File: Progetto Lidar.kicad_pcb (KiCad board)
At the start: 2 copper layers, 2 parts

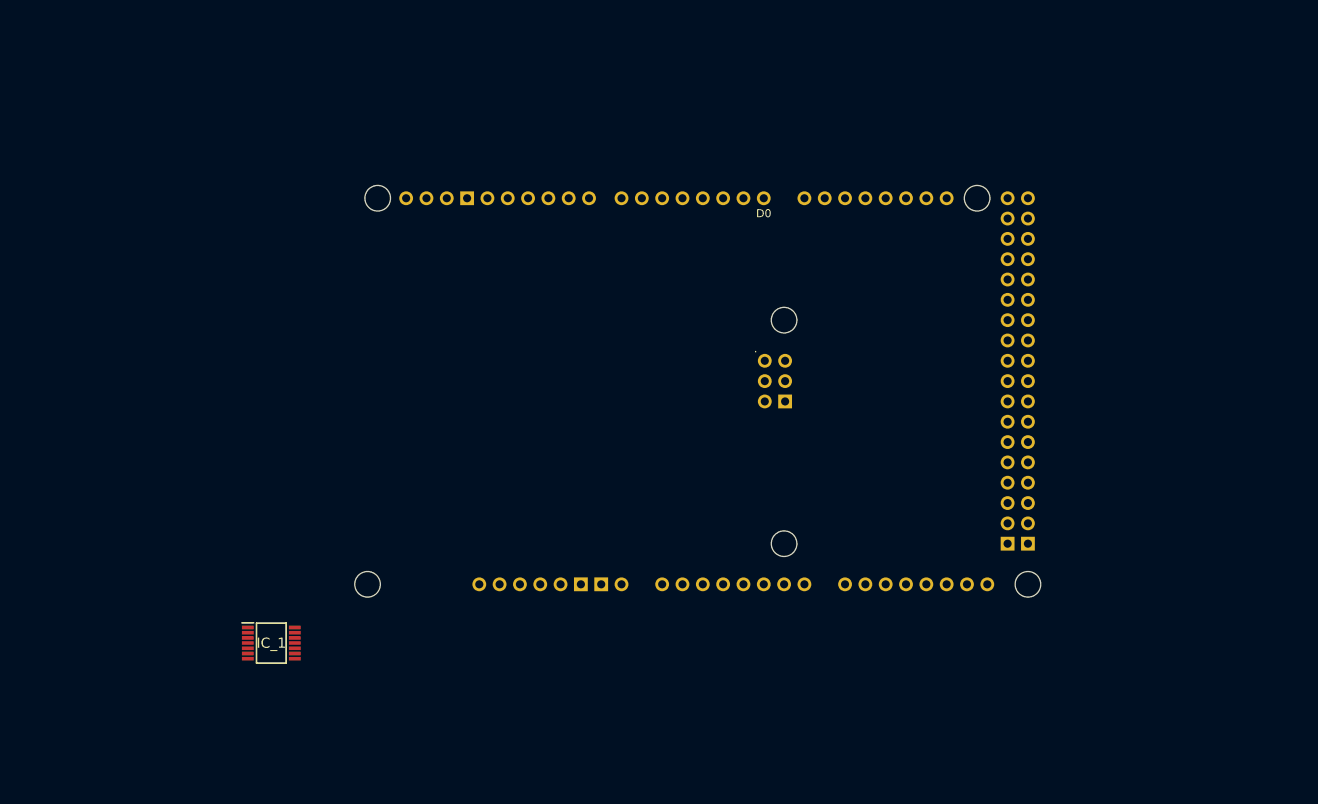
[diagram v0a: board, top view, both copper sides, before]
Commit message: Finito lo schematico e aggiunto modelli 3D
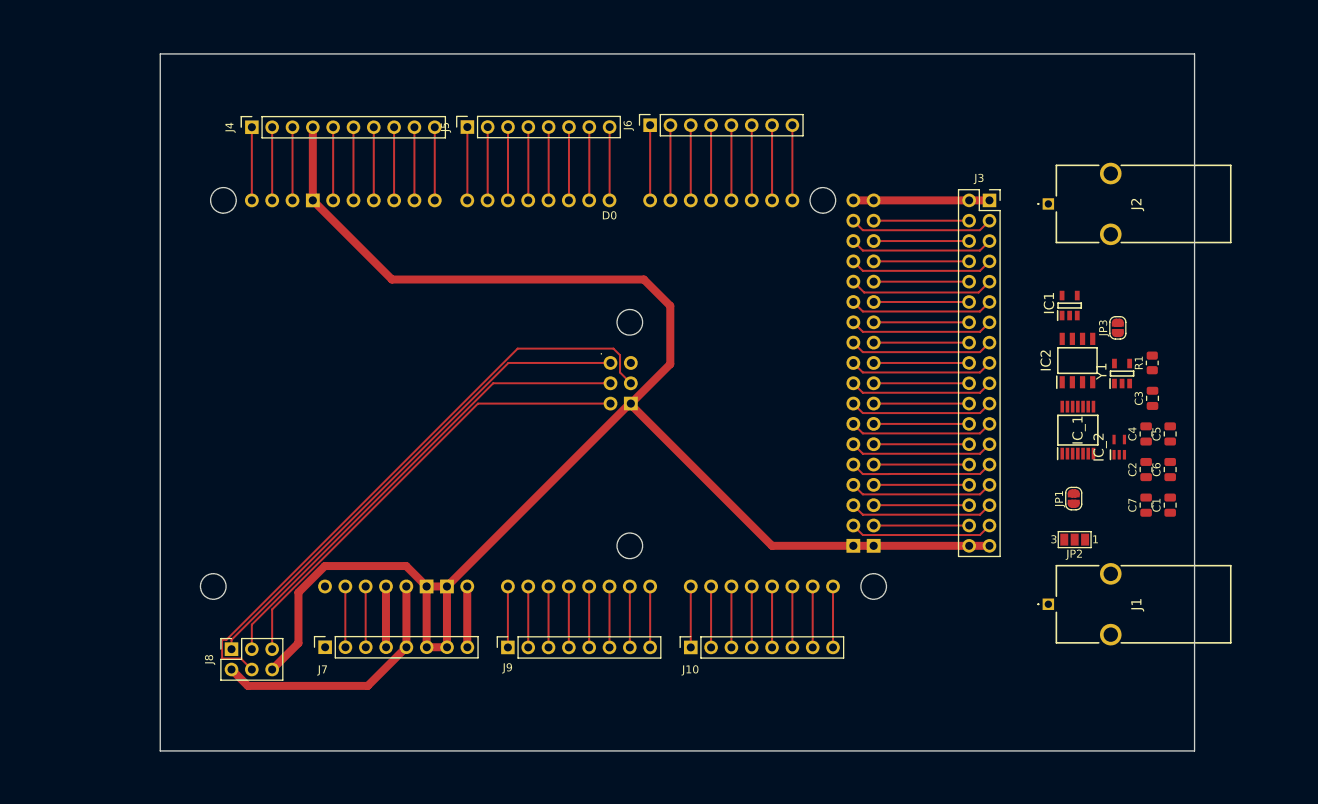
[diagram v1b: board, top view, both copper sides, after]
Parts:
- added C1: 0.1uF, Capacitor_SMD:C_0805_2012Metric, F.Cu at (207.8, 101.9)
- added C2: 1uF, Capacitor_SMD:C_0805_2012Metric, F.Cu at (204.8, 97.4)
- added C3: 100nF, Capacitor_SMD:C_0805_2012Metric, F.Cu at (205.6, 88.5)
- added C4: 1uF, Capacitor_SMD:C_0805_2012Metric, F.Cu at (204.8, 93.0)
- added C5: 100nF, Capacitor_SMD:C_0805_2012Metric, F.Cu at (207.8, 93.0)
- added C6: 100nF, Capacitor_SMD:C_0805_2012Metric, F.Cu at (207.8, 97.4)
- added C7: 100nF, Capacitor_SMD:C_0805_2012Metric, F.Cu at (204.8, 101.9)
- added IC1: TLV74133PDBVR, Libreria_componenti_footprint:SOT95P280X145-5N, F.Cu at (195.2, 76.9)
- added IC2: LM393BIDR, Libreria_componenti_footprint:SOIC127P600X175-8N, F.Cu at (196.2, 83.8)
- added IC_2: SN74LVC1G125DCKR, Libreria_componenti_footprint:SOT65P210X110-5N, F.Cu at (201.4, 94.6)
- added J1: CONN_LASER, Libreria_componenti_footprint:731713150, F.Cu at (192.5, 114.3)
- added J10: Conn_01x08, Connector_PinSocket_2.54mm:PinSocket_1x08_P2.54mm_Vertical, F.Cu at (147.8, 119.6)
- added J2: Conn_Coaxial, Libreria_componenti_footprint:731713150, F.Cu at (192.5, 64.2)
- added J3: Conn_02x18_Odd_Even, Connector_PinSocket_2.54mm:PinSocket_2x18_P2.54mm_Vertical, F.Cu at (185.2, 63.8)
- added J4: Conn_01x10, Connector_PinSocket_2.54mm:PinSocket_1x10_P2.54mm_Vertical, F.Cu at (93.0, 54.6)
- added J5: Conn_01x08, Connector_PinSocket_2.54mm:PinSocket_1x08_P2.54mm_Vertical, F.Cu at (119.9, 54.6)
- added J6: Conn_01x08, Connector_PinSocket_2.54mm:PinSocket_1x08_P2.54mm_Vertical, F.Cu at (142.8, 54.4)
- added J7: Conn_01x08, Connector_PinSocket_2.54mm:PinSocket_1x08_P2.54mm_Vertical, F.Cu at (102.1, 119.6)
- added J8: Conn_SPI, Connector_PinSocket_2.54mm:PinSocket_2x03_P2.54mm_Vertical, F.Cu at (90.4, 119.9)
- added J9: Conn_01x08, Connector_PinSocket_2.54mm:PinSocket_1x08_P2.54mm_Vertical, F.Cu at (125.0, 119.6)
- added JP1: REG_EN, Jumper:SolderJumper-2_P1.3mm_Open_RoundedPad1.0x1.5mm, F.Cu at (195.7, 101.0)
- added JP2: SolderJumper_3_Open, Jumper:SolderJumper-3_P1.3mm_Open_Pad1.0x1.5mm_NumberLabels, F.Cu at (195.8, 106.2)
- added JP3: OSC_EN, Jumper:SolderJumper-2_P1.3mm_Open_RoundedPad1.0x1.5mm, F.Cu at (201.2, 79.7)
- added R1: 10k, Resistor_SMD:R_0805_2012Metric, F.Cu at (205.5, 84.1)
- added Y1: SiT2024BA-S2-33E-8.000000G, Libreria_componenti_footprint:SOT95P280X145-5N, F.Cu at (201.8, 85.4)
- moved IC_1 104.3 mm to (196.2, 92.5), turned to 90 degrees
- moved A1 19.3 mm to (74.2, 114.6)
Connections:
- A1 pad 3V3: unconnected-(A1-Pad3V3) -> /3V3_ARDUINO
- A1 pad 5V1: unconnected-(A1-Pad5V1) -> +5V
- A1 pad 5V2: unconnected-(A1-Pad5V2) -> +5V
- A1 pad 5V3: unconnected-(A1-Pad5V3) -> +5V
- A1 pad 5V4: unconnected-(A1-Pad5V4) -> +5V
- A1 pad A0: unconnected-(A1-PadA0) -> /ARD_AN_A0
- A1 pad A1: unconnected-(A1-PadA1) -> /ARD_AN_A1
- A1 pad A10: unconnected-(A1-PadA10) -> /ARD_AN_A10
- A1 pad A11: unconnected-(A1-PadA11) -> /ARD_AN_A11
- A1 pad A2: unconnected-(A1-PadA2) -> /ARD_AN_A2
- A1 pad A3: unconnected-(A1-PadA3) -> /ARD_AN_A3
- A1 pad A4: unconnected-(A1-PadA4) -> /ARD_AN_A4
- A1 pad A5: unconnected-(A1-PadA5) -> /ARD_AN_A5
- A1 pad A6: unconnected-(A1-PadA6) -> /ARD_AN_A6
- A1 pad A7: unconnected-(A1-PadA7) -> /ARD_AN_A7
- A1 pad A8: unconnected-(A1-PadA8) -> /ARD_AN_A8
- A1 pad A9: unconnected-(A1-PadA9) -> /ARD_AN_A9
- A1 pad AREF: unconnected-(A1-PadAREF) -> /ARD_AN_AREF
- A1 pad CANR: unconnected-(A1-PadCANR) -> /ARD_CAN_RX
- A1 pad CANT: unconnected-(A1-PadCANT) -> /ARD_CAN_TX
- A1 pad D0: unconnected-(A1-PadD0) -> /ARD_SR_RX0
- A1 pad D1: unconnected-(A1-PadD1) -> /ARD_SR_TX0
- A1 pad D10: unconnected-(A1-PadD10) -> /ARD_GPIO_D10
- A1 pad D11: unconnected-(A1-PadD11) -> /ARD_GPIO_D11
- A1 pad D12: unconnected-(A1-PadD12) -> /ARD_GPIO_D12
- A1 pad D13: unconnected-(A1-PadD13) -> /ARD_GPIO_D13
- A1 pad D14: unconnected-(A1-PadD14) -> /ARD_SR_TX3
- A1 pad D15: unconnected-(A1-PadD15) -> /ARD_SR_RX3
- A1 pad D16: unconnected-(A1-PadD16) -> /ARD_SR_TX2
- A1 pad D17: unconnected-(A1-PadD17) -> /ARD_SR_RX2
- A1 pad D18: unconnected-(A1-PadD18) -> /ARD_SR_TX1
- A1 pad D19: unconnected-(A1-PadD19) -> /ARD_SR_RX1
- A1 pad D2: unconnected-(A1-PadD2) -> /SPI_CS
- A1 pad D20: unconnected-(A1-PadD20) -> /ARD_I2C_SDA
- A1 pad D21: unconnected-(A1-PadD21) -> /ARD_I2C_SCL
- A1 pad D22: unconnected-(A1-PadD22) -> /ARD_GPIO_D22
- A1 pad D23: unconnected-(A1-PadD23) -> /ARD_GPIO_D23
- A1 pad D24: unconnected-(A1-PadD24) -> /ARD_GPIO_D24
- A1 pad D25: unconnected-(A1-PadD25) -> /ARD_GPIO_D25
- A1 pad D26: unconnected-(A1-PadD26) -> /ARD_GPIO_D26
- A1 pad D27: unconnected-(A1-PadD27) -> /ARD_GPIO_D27
- A1 pad D28: unconnected-(A1-PadD28) -> /ARD_GPIO_D28
- A1 pad D29: unconnected-(A1-PadD29) -> /ARD_GPIO_D29
- A1 pad D3: unconnected-(A1-PadD3) -> /ARD_V_REF
- A1 pad D30: unconnected-(A1-PadD30) -> /ARD_GPIO_D30
- A1 pad D31: unconnected-(A1-PadD31) -> /ARD_GPIO_D31
- A1 pad D32: unconnected-(A1-PadD32) -> /ARD_GPIO_D32
- A1 pad D33: unconnected-(A1-PadD33) -> /ARD_GPIO_D33
- A1 pad D34: unconnected-(A1-PadD34) -> /ARD_GPIO_D34
- A1 pad D35: unconnected-(A1-PadD35) -> /ARD_GPIO_D35
- A1 pad D36: unconnected-(A1-PadD36) -> /ARD_GPIO_D36
- A1 pad D37: unconnected-(A1-PadD37) -> /ARD_GPIO_D37
- A1 pad D38: unconnected-(A1-PadD38) -> /ARD_GPIO_D38
- A1 pad D39: unconnected-(A1-PadD39) -> /ARD_GPIO_D39
- A1 pad D4: unconnected-(A1-PadD4) -> /ARD_TRIG
- A1 pad D40: unconnected-(A1-PadD40) -> /ARD_GPIO_D40
- A1 pad D41: unconnected-(A1-PadD41) -> /ARD_GPIO_D41
- A1 pad D42: unconnected-(A1-PadD42) -> /ARD_GPIO_D42
- A1 pad D43: unconnected-(A1-PadD43) -> /ARD_GPIO_D43
- A1 pad D44: unconnected-(A1-PadD44) -> /ARD_GPIO_D44
- A1 pad D45: unconnected-(A1-PadD45) -> /ARD_GPIO_45
- A1 pad D46: unconnected-(A1-PadD46) -> /ARD_GPIO_46
- A1 pad D47: unconnected-(A1-PadD47) -> /ARD_GPIO_47
- A1 pad D48: unconnected-(A1-PadD48) -> /ARD_GPIO_48
- A1 pad D49: unconnected-(A1-PadD49) -> /ARD_GPIO_49
- A1 pad D5: unconnected-(A1-PadD5) -> /ARD_BUFF_EN
- A1 pad D50: unconnected-(A1-PadD50) -> /ARD_GPIO_50
- A1 pad D51: unconnected-(A1-PadD51) -> /ARD_GPIO_51
- A1 pad D52: unconnected-(A1-PadD52) -> /ARD_GPIO_52
- A1 pad D53: unconnected-(A1-PadD53) -> /ARD_GPIO_D53
- A1 pad D6: unconnected-(A1-PadD6) -> /ARD_GPIO_D6
- A1 pad D7: unconnected-(A1-PadD7) -> /ARD_GPIO_D7
- A1 pad D8: unconnected-(A1-PadD8) -> /ARD_GPIO_D8
- A1 pad D9: unconnected-(A1-PadD9) -> /ARD_GPIO_D9
- A1 pad DAC0: unconnected-(A1-PadDAC0) -> /ARD_AN_DAC0
- A1 pad DAC1: unconnected-(A1-PadDAC1) -> /ARD_AN_DAC1
- A1 pad GND1: unconnected-(A1-PadGND1) -> GND
- A1 pad GND2: unconnected-(A1-PadGND2) -> GND
- A1 pad GND3: unconnected-(A1-PadGND3) -> GND
- A1 pad GND4: unconnected-(A1-PadGND4) -> GND
- A1 pad GND5: unconnected-(A1-PadGND5) -> GND
- A1 pad GND6: unconnected-(A1-PadGND6) -> GND
- A1 pad IORF: unconnected-(A1-PadIORF) -> /ARD_AN_IORF
- A1 pad MISO: unconnected-(A1-PadMISO) -> /SPI_MISO
- A1 pad MOSI: unconnected-(A1-PadMOSI) -> /SPI_MOSI
- A1 pad RST1: unconnected-(A1-PadRST1) -> /ARD_AN_RST1
- A1 pad RST2: unconnected-(A1-PadRST2) -> /SPI_RESET
- A1 pad SCK: unconnected-(A1-PadSCK) -> /SPI_SCK
- A1 pad SCL1: unconnected-(A1-PadSCL1) -> /ARD_I2C_SCL1
- A1 pad SDA1: unconnected-(A1-PadSDA1) -> /ARD_I2C_SDA1
- A1 pad VIN: unconnected-(A1-PadVIN) -> /ARD_VIN
- IC_1 pad 1: unconnected-(IC_1-Pad1) -> /SPI_CS
- IC_1 pad 10: unconnected-(IC_1-Pad10) -> /SPI_MOSI
- IC_1 pad 11: unconnected-(IC_1-Pad11) -> /SPI_CS
- IC_1 pad 12: unconnected-(IC_1-Pad12) -> /SPI_SCK
- IC_1 pad 13: unconnected-(IC_1-Pad13) -> Net-(C4-Pad1)
- IC_1 pad 14: unconnected-(IC_1-Pad14) -> Net-(C3-Pad2)
- IC_1 pad 2: unconnected-(IC_1-Pad2) -> /ARD_TRIG
- IC_1 pad 3: unconnected-(IC_1-Pad3) -> /TDC_START
- IC_1 pad 4: unconnected-(IC_1-Pad4) -> /TDC_STOP
- IC_1 pad 5: unconnected-(IC_1-Pad5) -> /TDC_CLOCK
- IC_1 pad 7: unconnected-(IC_1-Pad7) -> GND
- IC_1 pad 9: unconnected-(IC_1-Pad9) -> /SPI_MISO
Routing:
- net GND: track 0.00 -> 208.0 mm
- net /SPI_MOSI: track 0.00 -> 75.9 mm
- net /SPI_MISO: track 0.00 -> 62.9 mm
- net /SPI_SCK: track 0.00 -> 60.4 mm
- net /SPI_RESET: track 0.00 -> 57.9 mm
- net +5V: track 0.00 -> 49.3 mm
- net /ARD_GPIO_D28: track 0.00 -> 18.1 mm
- net /ARD_GPIO_D44: track 0.00 -> 18.0 mm
- net /ARD_GPIO_D40: track 0.00 -> 18.0 mm
- net /ARD_GPIO_D36: track 0.00 -> 18.0 mm
- net /ARD_GPIO_D30: track 0.00 -> 18.0 mm
- net /ARD_GPIO_D26: track 0.00 -> 18.0 mm
- net /ARD_GPIO_D22: track 0.00 -> 18.0 mm
- net /ARD_GPIO_48: track 0.00 -> 18.0 mm
- net /ARD_GPIO_D42: track 0.00 -> 18.0 mm
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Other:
- board outline added: 129.3 x 87.1 mm

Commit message: Finito il layout della prima versione della scheda
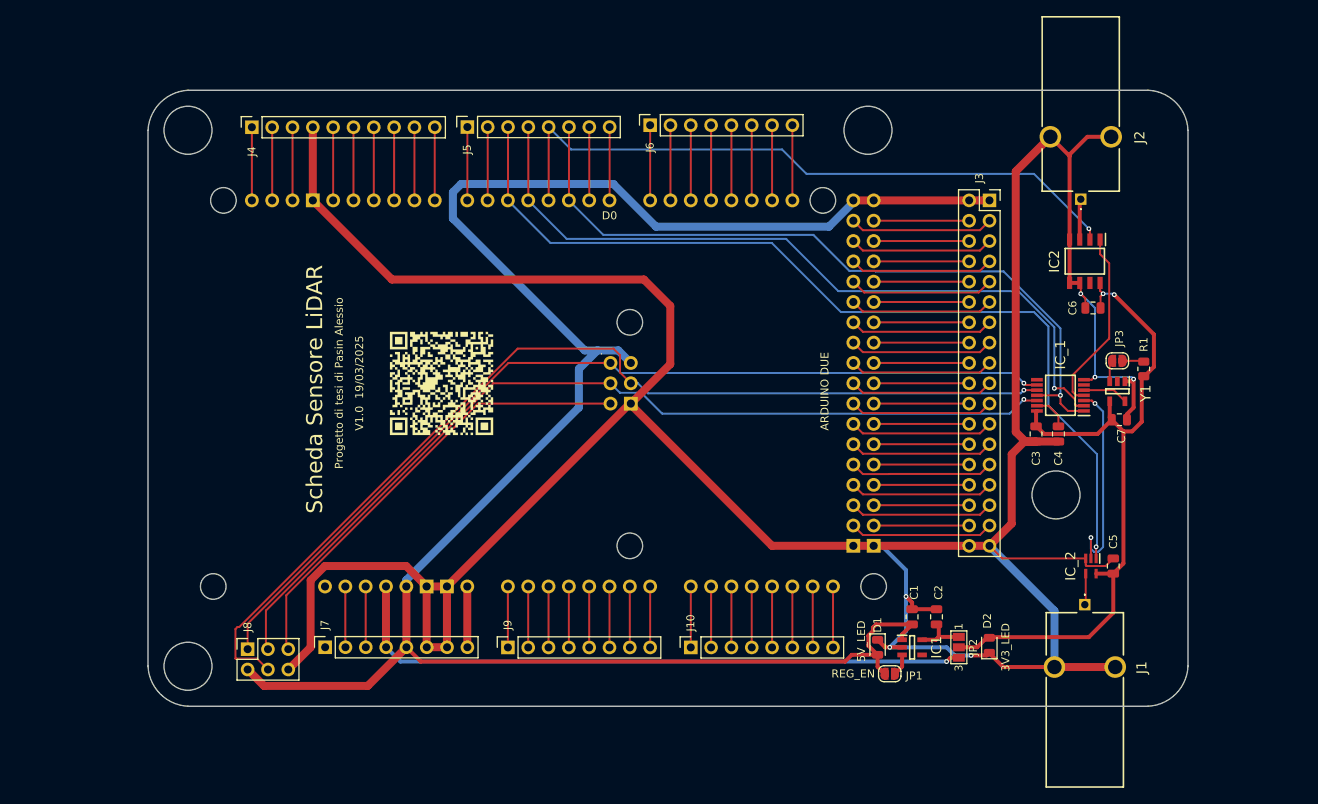
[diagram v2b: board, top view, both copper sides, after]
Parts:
- added D1: 5V_LED, LED_SMD:LED_0805_2012Metric, F.Cu at (171.2, 119.6)
- added D2: 3V3_LED, LED_SMD:LED_0805_2012Metric, F.Cu at (185.2, 119.4)
- moved IC1 47.0 mm to (175.5, 119.6), turned to 0 degrees
- moved C1 35.1 mm to (175.5, 115.8)
- moved C2 32.0 mm to (178.6, 115.8)
- moved JP1 31.7 mm to (172.7, 122.9), turned to 180 degrees
- moved C6 22.4 mm to (198.1, 77.2), turned to 180 degrees
- moved JP2 19.8 mm to (181.4, 119.6), turned to -90 degrees
- moved C5 18.0 mm to (200.7, 109.5)
- moved IC_2 15.3 mm to (197.9, 109.5), turned to -90 degrees
- moved C3 15.2 mm to (191.0, 93.0), turned to -90 degrees
- moved IC2 12.4 mm to (197.1, 71.4), turned to -90 degrees
- moved C7 11.2 mm to (201.4, 91.2), turned to 0 degrees
- moved C4 11.0 mm to (193.8, 93.0), turned to -90 degrees
- moved IC_1 4.86 mm to (194.1, 88.1), turned to 180 degrees
- moved J1 4.56 mm to (197.1, 114.3), turned to 0 degrees
- moved JP3 4.12 mm to (201.2, 83.8), turned to 0 degrees
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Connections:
- C3 pad 2: Net-(C3-Pad2) -> GND
- IC_1 pad 14: Net-(C3-Pad2) -> +3V3
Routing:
- net GND: track 208.0 -> 412.1 mm, vias 0 -> 6
- net +5V: track 49.3 -> 248.2 mm
- net /ARD_BUFF_EN: track 9.18 -> 114.8 mm, vias 0 -> 1
- net +3V3: track 0.00 -> 89.9 mm, vias 0 -> 2
- net /ARD_TRIG: track 9.18 -> 94.1 mm, vias 0 -> 1
- net /SPI_CS: track 9.18 -> 92.9 mm, vias 0 -> 1
- net /ARD_V_REF: track 9.18 -> 83.4 mm, vias 0 -> 1
- net /3V3_ARDUINO: track 7.60 -> 80.1 mm, vias 0 -> 1
- net /SPI_SCK: track 60.4 -> 115.4 mm, vias 0 -> 1
- net /SPI_MISO: track 62.9 -> 116.5 mm, vias 0 -> 1
- net /SPI_MOSI: track 75.9 -> 126.8 mm, vias 0 -> 1
- net /TDC_START: track 0.00 -> 25.8 mm, vias 0 -> 2
- net /TDC_STOP: track 0.00 -> 23.0 mm
- net Net-(C2-Pad1): track 0.00 -> 6.41 mm
- net /TDC_CLOCK: track 0.00 -> 5.70 mm
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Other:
- board size 129.3 x 87.1 mm -> 130 x 77 mm
- board text added: "Progetto di tesi di Pasin Alessio"
- board text added: "Scheda Sensore LiDAR"
- board text added: "V1.0 19/03/2025"

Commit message: Specchiato Arduino per funzionare con connettori femmina
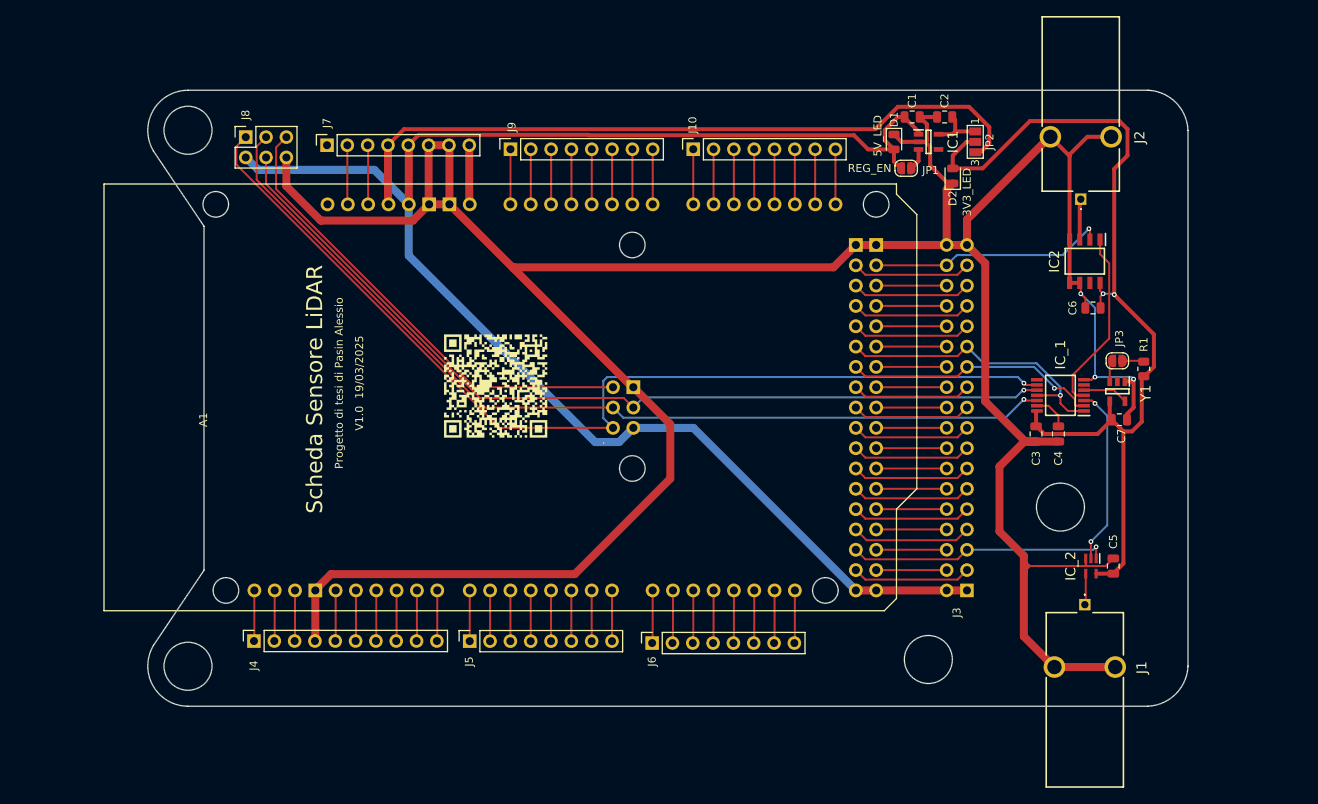
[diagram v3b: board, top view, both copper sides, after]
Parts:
- A1, J3: moved to B.Cu
- moved J6 64.7 mm to (143.0, 119.1)
- moved J5 64.3 mm to (120.2, 118.9)
- moved J4 64.2 mm to (93.2, 118.8)
- moved J8 64.0 mm to (92.2, 55.9)
- moved D1 63.2 mm to (173.2, 56.5)
- moved JP1 63.2 mm to (174.8, 59.8)
- moved IC1 63.2 mm to (177.6, 56.5)
- moved JP2 63.2 mm to (183.4, 56.5)
- moved J7 62.8 mm to (102.4, 56.9)
- moved C2 62.5 mm to (179.6, 53.3), turned to 180 degrees
- moved C1 62.5 mm to (175.5, 53.3), turned to 0 degrees
- moved J9 62.3 mm to (125.3, 57.4)
- moved J10 62.3 mm to (148.2, 57.4)
- moved D2 58.9 mm to (180.6, 60.7)
- moved A1 52.8 mm to (74.5, 61.7)
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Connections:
- A1 pad D2: /SPI_CS -> /ARD_GPIO_D2
- A1 pad D24: /ARD_GPIO_D24 -> /ARD_BUFF_EN
- A1 pad D3: /ARD_V_REF -> /ARD_GPIO_D3
- A1 pad D4: /ARD_TRIG -> /ARD_GPIO_D4
- A1 pad D42: /ARD_GPIO_D42 -> /ARD_TRIG
- A1 pad D44: /ARD_GPIO_D44 -> /SPI_CS
- A1 pad D5: /ARD_BUFF_EN -> /ARD_GPIO_D5
- A1 pad D53: /ARD_GPIO_D53 -> /ARD_V_REF
- J3 pad 23: /ARD_GPIO_D42 -> /ARD_TRIG
- J3 pad 25: /ARD_GPIO_D44 -> /SPI_CS
- J3 pad 34: /ARD_GPIO_D53 -> /ARD_V_REF
- J3 pad 5: /ARD_GPIO_D24 -> /ARD_BUFF_EN
- J5 pad 3: /ARD_BUFF_EN -> /ARD_GPIO_D5
- J5 pad 4: /ARD_TRIG -> /ARD_GPIO_D4
- J5 pad 5: /ARD_V_REF -> /ARD_GPIO_D3
- J5 pad 6: /SPI_CS -> /ARD_GPIO_D2
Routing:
- net /ARD_BUFF_EN: track 114.8 -> 32.6 mm
- net /ARD_TRIG: track 94.1 -> 32.0 mm
- net /SPI_CS: track 92.9 -> 37.0 mm
- net /ARD_V_REF: track 83.4 -> 29.9 mm
- net +5V: track 248.2 -> 198.9 mm
- net +3V3: track 89.9 -> 115.1 mm
- net GND: track 412.1 -> 390.1 mm, vias 6 -> 3
- net /ARD_GPIO_D44: track 18.0 -> 0.00 mm
- net /ARD_GPIO_D42: track 18.0 -> 0.00 mm
- net /ARD_GPIO_D24: track 18.0 -> 0.00 mm
- net /SPI_MOSI: track 126.8 -> 112.2 mm
- net /ARD_GPIO_D53: track 11.9 -> 0.00 mm
- net /3V3_ARDUINO: track 80.1 -> 89.9 mm, vias 1 -> 0
- net /SPI_MISO: track 116.5 -> 125.8 mm
- net /ARD_GPIO_D4: track 0.00 -> 6.34 mm
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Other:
- outline, holes or cut-outs redrawn

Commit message: Apportate modifiche dopo incontro con prof. 25.03.2025
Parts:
- added C8: 1nF, Capacitor_SMD:C_0805_2012Metric, F.Cu at (196.1, 116.1)
- added C9: 1nF, Capacitor_SMD:C_0805_2012Metric, F.Cu at (197.6, 66.8)
- added R2: 1k8, Resistor_SMD:R_0805_2012Metric, F.Cu at (173.2, 47.0)
- added R3: 820, Resistor_SMD:R_0805_2012Metric, F.Cu at (181.8, 46.5)
- IC2: value LM393BIDR -> LT1719IS6#TRPBF; footprint Libreria_componenti_footprint:SOIC127P600X175-8N -> Libreria_componenti_footprint:SOT95P280X100-6N
- J1, J2: footprint Libreria_componenti_footprint:731713150 -> Connector_Coaxial:SMA_Molex_73251-1153_EdgeMount_Horizontal
- moved D2 16.0 mm to (177.4, 45.0), turned to 0 degrees
- moved C6 12.7 mm to (197.6, 64.5), turned to 0 degrees
- moved D1 12.1 mm to (170.2, 44.7), turned to 0 degrees
- moved J1 10.6 mm to (205.5, 108.0), turned to 180 degrees
- moved J2 10.5 mm to (205.7, 68.8)
- moved IC2 1.37 mm to (197.6, 70.1), turned to 180 degrees
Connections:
- A1 pad D53: /ARD_V_REF -> /ARD_GPIO_53
- A1 pad DAC0: /ARD_AN_DAC0 -> /ARD_V_REF
- D1 pad 2: +5V -> Net-(D1-Pad2)
- D2 pad 2: +3V3 -> Net-(D2-Pad2)
- IC2 pad 1: /TDC_STOP -> /ARD_V_REF
- IC2 pad 2: /ARD_V_REF -> GND
- IC2 pad 4: GND -> +3V3
- IC2 pad 5: GND -> /TDC_STOP
- J10 pad 5: /ARD_AN_DAC0 -> /ARD_V_REF
- J3 pad 34: /ARD_V_REF -> /ARD_GPIO_53
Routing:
- net GND: track 390.1 -> 324.1 mm, vias 3 -> 2
- net +3V3: track 115.1 -> 62.3 mm, vias 2 -> 0
- net /ARD_V_REF: track 29.9 -> 6.89 mm, vias 1 -> 0
- net /TDC_STOP: track 23.0 -> 10.2 mm
- net /ARD_GPIO_53: track 0.00 -> 10.6 mm
- net /ARD_AN_DAC0: track 6.89 -> 0.00 mm
- net /RIC_STOP: track 5.10 -> 0.00 mm
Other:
- outline, holes or cut-outs redrawn
